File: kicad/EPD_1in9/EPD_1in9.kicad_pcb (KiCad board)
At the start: 2 copper layers, 34 x 51 mm, 11 parts, among them J1 Conn_01x02, J2 Conn_01x08, J3 Conn_01x08, J4 Conn_01x08

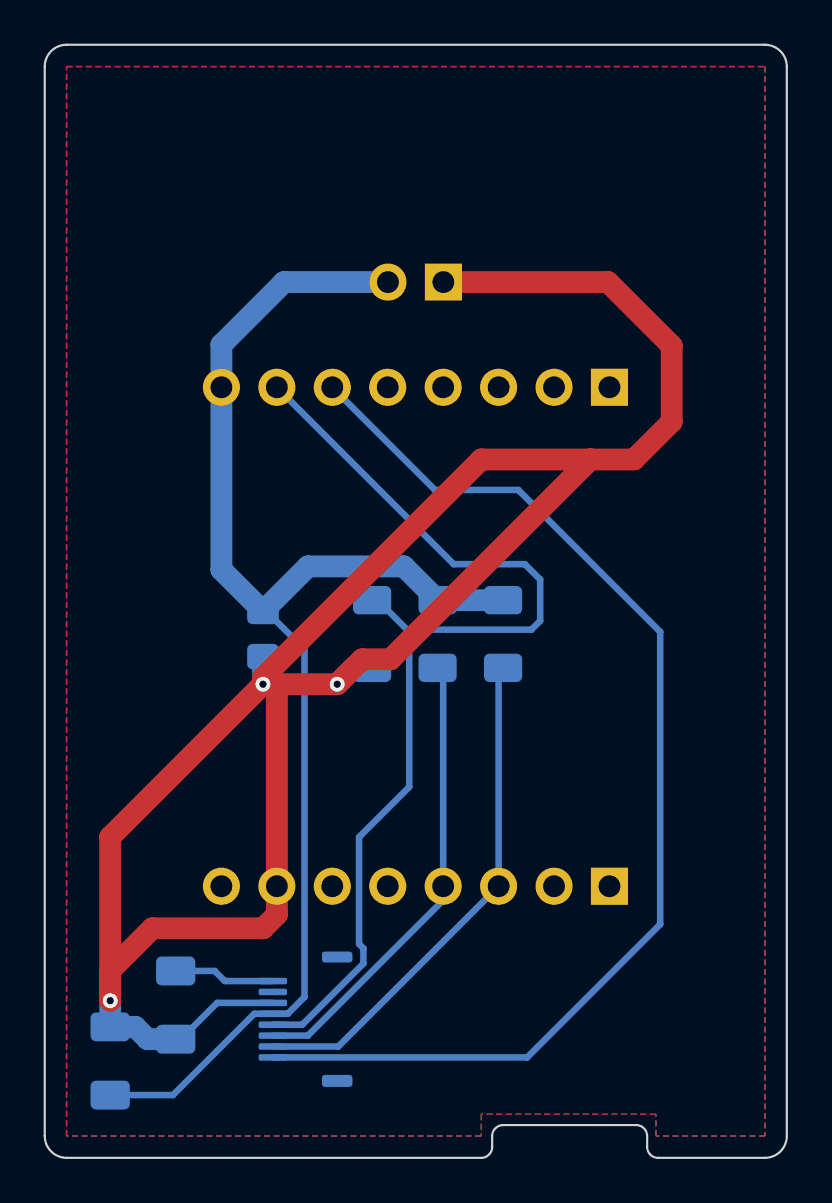
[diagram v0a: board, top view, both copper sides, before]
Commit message: EPD_1in9: Create Rev C circuit board
Updates based on assembly of Rev A boards
-Add labels for the D1-mini pin headers
-Change pin-headers from THT to SMD
 (Note: the 2 pin horizontal connector doesn't have a proper 3D-model)
-Remove large tracks from 3V3 and GND pads and enable thermal reliefs in
 the filled zones
-Update display footprint to better show where the cable folds on the fab
 layer (this also matches the 3D-model)
-Move FPC connector based on where the cable folds to (this also matches
 the 3D-model of the screen better)
-Increase size of routed slot at bottom of board slightly
-Add keepout zone around the HV nets
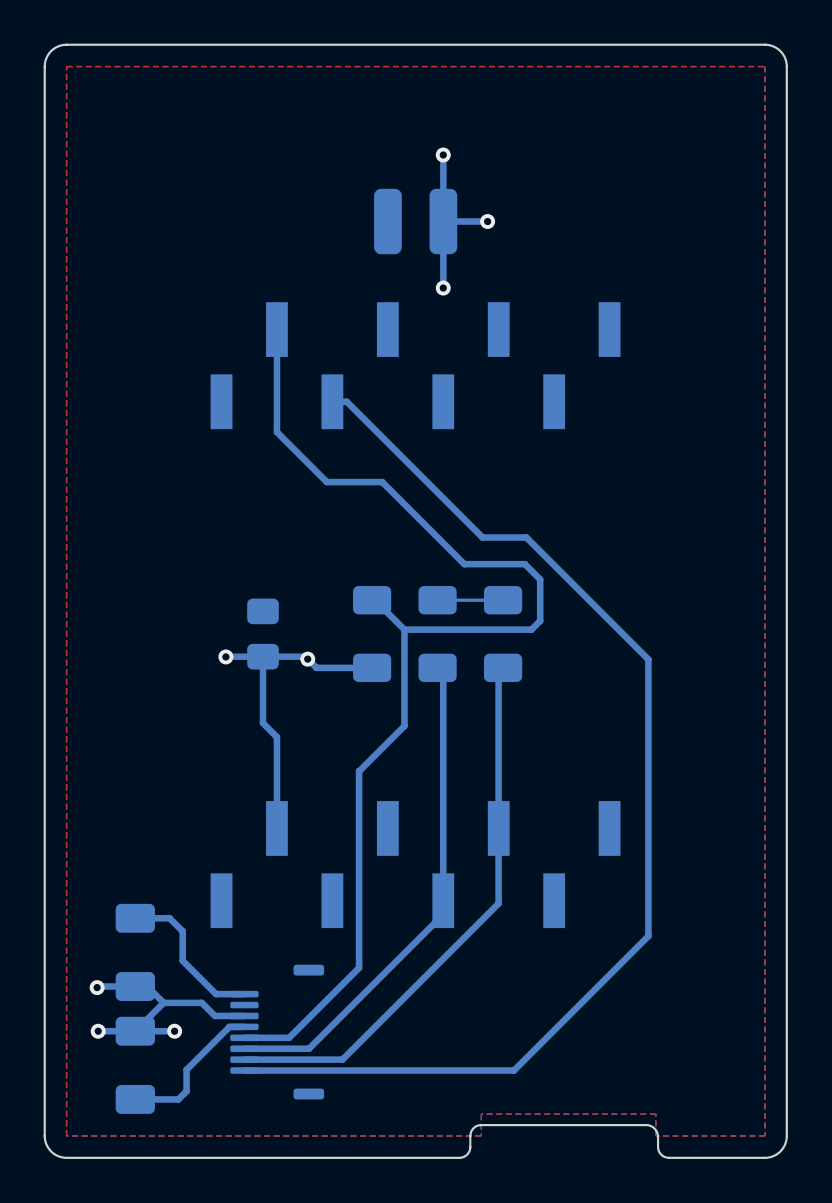
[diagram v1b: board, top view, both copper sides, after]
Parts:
- J1: footprint Connector_PinHeader_2.54mm:PinHeader_1x02_P2.54mm_Horizontal -> Connector_local:PinHeader_1x02_P2.54mm_Horizontal_SMD
- J2, J3: footprint Connector_PinSocket_2.54mm:PinSocket_1x08_P2.54mm_Vertical -> Connector_PinHeader_2.54mm:PinHeader_1x08_P2.54mm_Vertical_SMD_Pin1Right
- moved J3 8.94 mm to (47.0, 67.6)
- moved J2 8.94 mm to (47.0, 44.7)
- moved C3 3.04 mm to (34.1, 71.6)
- moved J1 2.77 mm to (48.3, 38.1)
- moved J4 1.43 mm to (40.4, 75.2)
- moved C2 1.17 mm to (34.1, 76.8)
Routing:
- net GND: track 109.2 -> 35.8 mm, vias 3 -> 8
- net +3.3V: track 63.6 -> 9.95 mm
- net /~{RESET}: track 47.7 -> 52.8 mm
- net /HV: track 4.64 -> 7.23 mm
- net /SCL: track 23.5 -> 25.5 mm
- net /SDA: track 21.1 -> 23.1 mm
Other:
- outline, holes or cut-outs redrawn
- board text added: "3V3"
- board text added: "EPD_1in9 Rev C"
- board text added: "GND"
- board text added: "RST A0 D0 D5 D6 D7 D8 3V3"
- board text added: "TX RX D1 D2 D3 D4 GND 5V"
- board text removed: "EPD_1in9 Rev B"

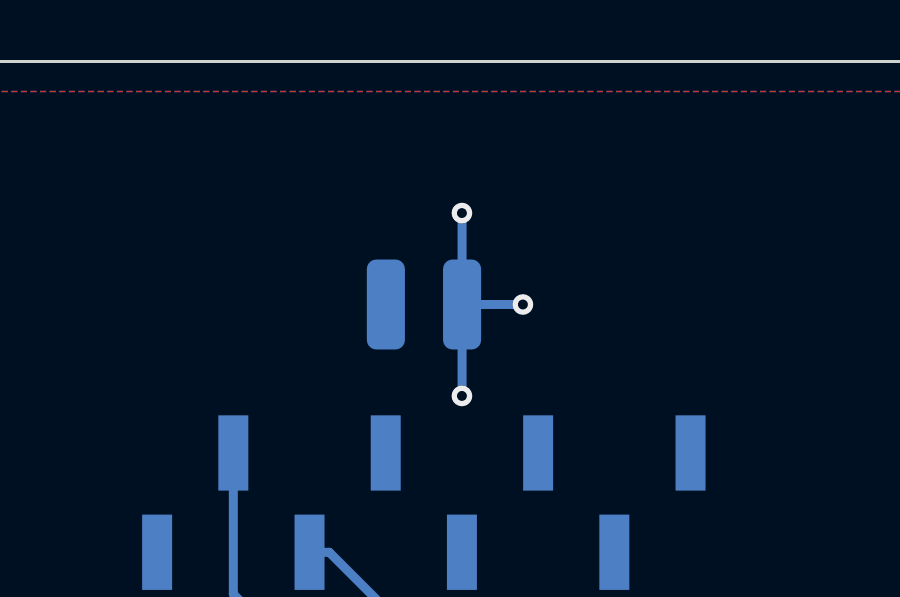
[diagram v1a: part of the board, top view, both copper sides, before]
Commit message: EPD_1in9: Create Rev D circuit board
Just switch from right-angle power input header to normal vertical header.
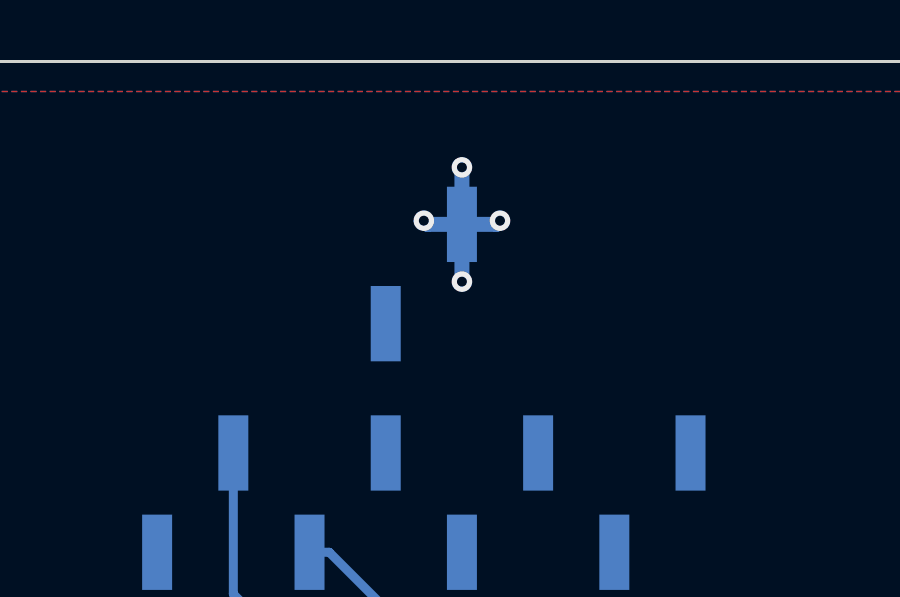
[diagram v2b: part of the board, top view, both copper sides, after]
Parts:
- J1: footprint Connector_local:PinHeader_1x02_P2.54mm_Horizontal_SMD -> Connector_PinHeader_2.54mm:PinHeader_1x02_P2.54mm_Vertical_SMD_Pin1Right
- moved J1 1.63 mm to (47.0, 37.1)
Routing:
- net GND: track 35.8 -> 34.4 mm, vias 8 -> 9
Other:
- board text added: "EPD_1in9 Rev D"
- board text removed: "EPD_1in9 Rev C"
